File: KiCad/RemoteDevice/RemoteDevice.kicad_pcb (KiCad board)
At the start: 2 copper layers, 99.5 x 59.2 mm, 42 parts, among them J1 Alim, J2 CN1, Q1 Si4435, SW1 BP, SW2 BP, U1 XC9140, U2 STM32L041F6Px, U3 MCP6281, U4 ADT7410TRZ, U5 MCP6281, U6 RT606, U7 Microphone

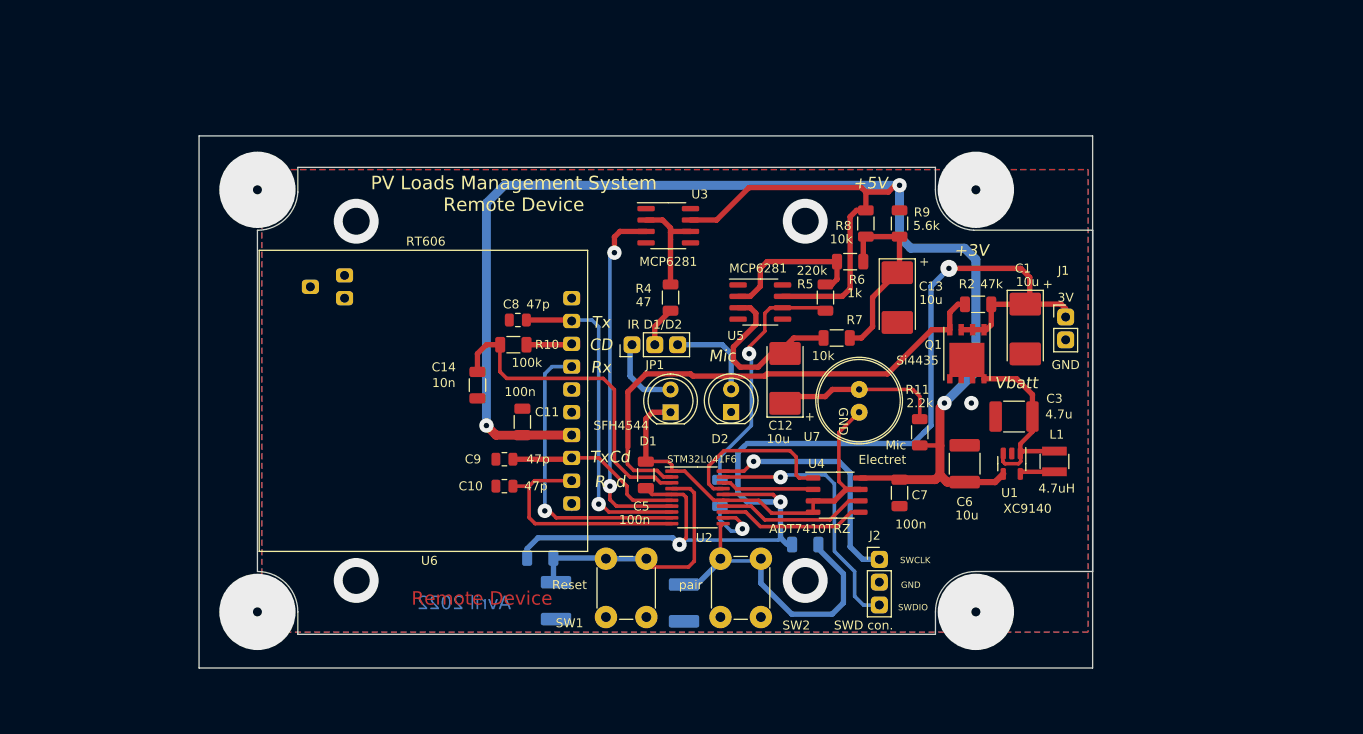
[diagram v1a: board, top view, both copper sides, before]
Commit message: routage commencé. ALim OK placer les deux diodes, étudier l'alim particulière uC et Temp Sensor
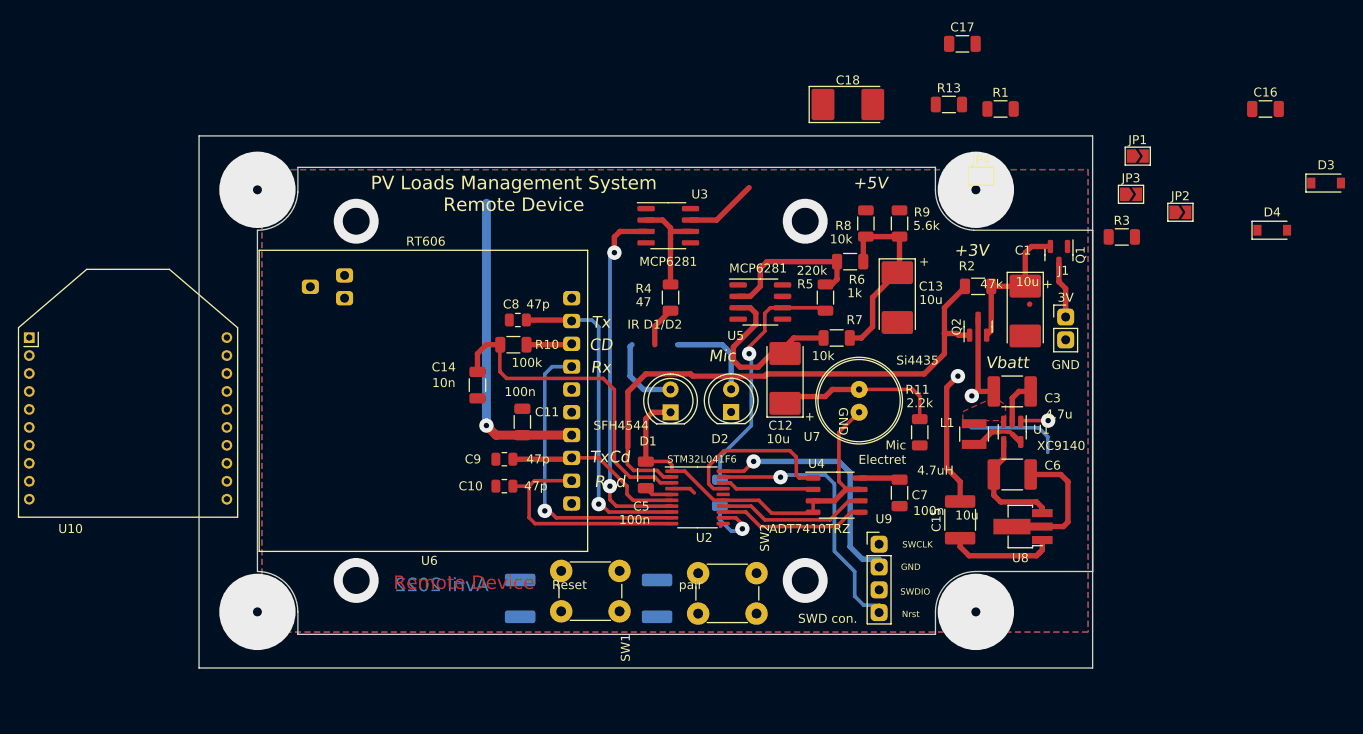
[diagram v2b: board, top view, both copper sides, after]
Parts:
- removed J2: CN1, LibKiCad_PjtDeviceManagePV:PinHeader3pts
- added C15: 10u, Capacitor_SMD:C_1812_4532Metric, F.Cu at (106.2, 102.2)
- added C16: 100n, Capacitor_SMD:C_1206_3216Metric, F.Cu at (140.2, 56.5)
- added C17: 10n, Capacitor_SMD:C_1206_3216Metric, F.Cu at (106.5, 49.2)
- added C18: 10u, Capacitor_Tantalum_SMD:CP_EIA-7132-20_AVX-U, F.Cu at (93.8, 56.0)
- added D3: BAT43W-V, Diode_SMD:D_SOD-123, F.Cu at (147.0, 64.8)
- added D4: BAT43W-V, Diode_SMD:D_SOD-123, F.Cu at (141.0, 70.0)
- added JP2: SolderJumper_2_Open, Jumper:SolderJumper-2_P1.3mm_Open_TrianglePad1.0x1.5mm, F.Cu at (130.8, 68.0)
- added JP3: SolderJumper_2_Open, Jumper:SolderJumper-2_P1.3mm_Open_TrianglePad1.0x1.5mm, F.Cu at (125.3, 66.0)
- added JP4: SolderJumper_2_Open, Jumper:SolderJumper-2_P1.3mm_Open_TrianglePad1.0x1.5mm, F.Cu at (108.6, 64.0)
- added Q2: Q_PMOS_GSD, Package_TO_SOT_SMD:SOT-23, F.Cu at (108.2, 80.8)
- added R13: 2.2k, Resistor_SMD:R_1206_3216Metric, F.Cu at (105.0, 56.0)
- added U10: XBEE-3, LibKiCad_INSA:XBEE-3-TH, F.Cu at (1.40, 102.0)
- added U8: LD2981CU33, Package_TO_SOT_SMD:SOT-89-3_Handsoldering, F.Cu at (113.2, 103.0)
- added U9: Con_4pts, LibKiCad_PjtDeviceManagePV:PinHeader4pts, F.Cu at (97.5, 107.8)
- JP1: value 3pts -> SolderJumper_2_Open; footprint LibKiCad_PjtDeviceManagePV:PinHeader3pts -> Jumper:SolderJumper-2_P1.3mm_Open_TrianglePad1.0x1.5mm
- Q1: value Si4435 -> Q_PMOS_GSD; footprint Package_SO:PowerPAK_SO-8_Single -> Package_TO_SOT_SMD:SOT-23
- R1: value R -> 10k; moved to F.Cu
- R3: value 4.7k -> 10k; moved to F.Cu
- moved R1 71.6 mm to (110.8, 56.5)
- moved JP1 57.7 mm to (126.0, 61.8), turned to 0 degrees
- moved R3 49.1 mm to (124.2, 70.8)
- moved Q1 15.0 mm to (117.2, 72.8)
- moved L1 9.46 mm to (107.8, 92.7)
- moved C6 5.43 mm to (112.0, 97.2), turned to 0 degrees
- moved SW1 4.03 mm to (65.0, 110.2), turned to 180 degrees
- moved C2 4.01 mm to (57.2, 111.0)
- moved U1 3.55 mm to (112.0, 92.5)
- moved C4 3.04 mm to (72.5, 111.0)
- moved C3 2.81 mm to (112.0, 88.0), turned to 0 degrees
- moved C1 2.00 mm to (113.5, 79.0)
- moved R2 2.00 mm to (108.2, 76.2)
- moved SW2 1.68 mm to (80.2, 110.5), turned to 180 degrees
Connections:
- C1 pad 1: +3V0 -> Net-(C1-Pad1)
- C5 pad 1: +3V0 -> VDD
- C7 pad 1: +5V -> /Pwr_ADT7410
- JP1 pad 1: /LED_Top -> /Pwr_ADT7410
- JP1 pad 2: /LED -> +3V3
- Q1 pad 1: +3V0 -> GND
- Q1 pad 2: +3V0 -> Net-(C1-Pad1)
- R1 pad 1: +3V0 -> /Pwr_ADT7410
- R1 pad 2: /Reset -> /SCL
- R11 pad 1: +5V -> Net-(C18-Pad1)
- R2 pad 1: +3V0 -> Net-(C1-Pad1)
- R3 pad 1: +3V0 -> /Pwr_ADT7410
- R3 pad 2: /UserBP -> /SDA
- R8 pad 1: +5V -> +3V3
- U2 pad 16: +3V0 -> VDD
- U2 pad 5: +3V0 -> VDD
- U3 pad 7: +5V -> +3V3
- U4 pad 8: +5V -> /Pwr_ADT7410
- U5 pad 7: +5V -> +3V3
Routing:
- net +5V: track 187.0 -> 47.7 mm, vias 3 -> 1
- net +3V0: track 131.6 -> 6.29 mm, vias 3 -> 0
- net /UserBP: track 35.2 -> 0.43 mm
- net GND: track 47.1 -> 79.2 mm
- net /Reset: track 29.7 -> 2.71 mm
- net +3V3: track 0.00 -> 20.1 mm
- net Net-(C1-Pad1): track 0.00 -> 16.3 mm
- net /BoostEn: track 56.4 -> 62.1 mm
- net /Vbatt: track 21.2 -> 26.3 mm, vias 0 -> 2
- net /Pwr_ADT7410: track 0.00 -> 4.45 mm
- net VDD: track 0.00 -> 3.18 mm
- net /Lx: track 3.90 -> 6.25 mm
- added copper zone on F.Cu, net /Vbatt
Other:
- board text added: "Nrst"

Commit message: Reste la partie Xbee et les résistances de pull up. Bien penser aussi les plans de masse alim...
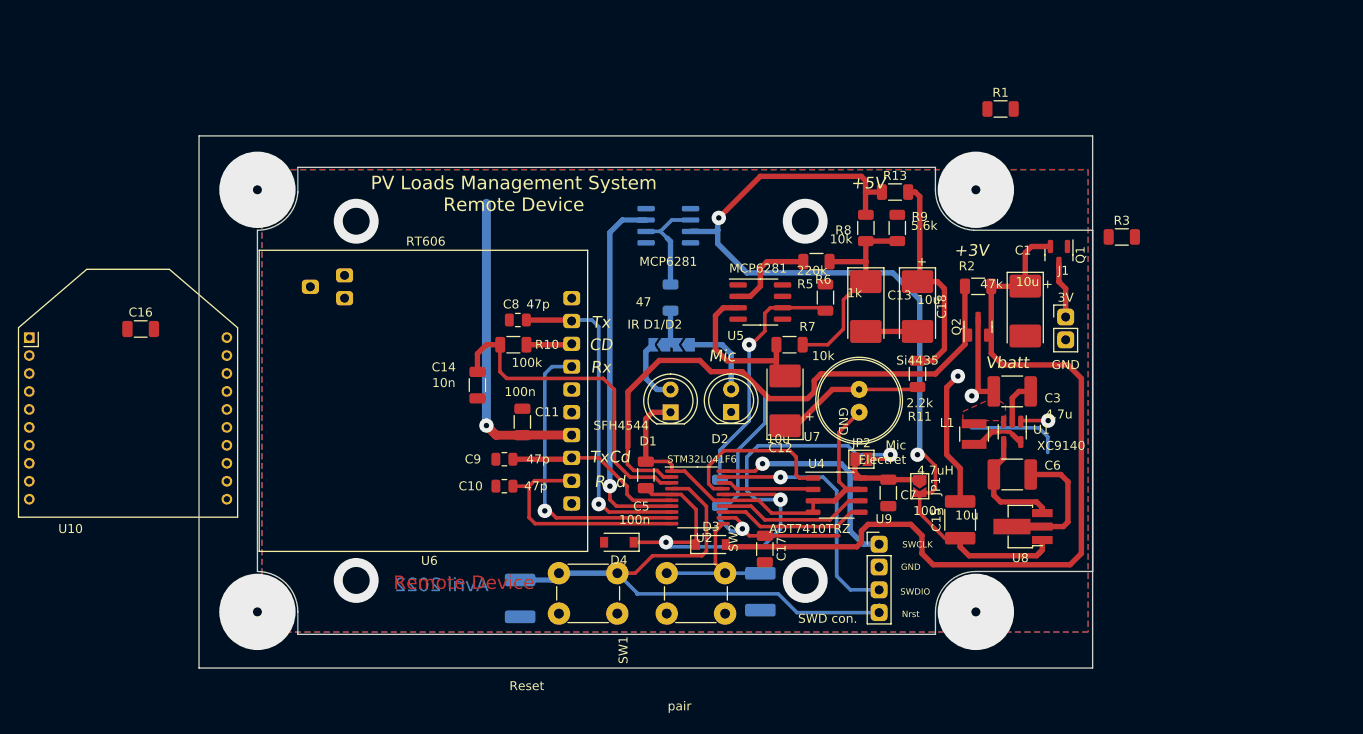
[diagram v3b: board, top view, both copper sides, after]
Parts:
- JP3, JP4, R4, U3: moved to B.Cu
- moved C16 127.6 mm to (15.0, 81.0)
- moved D4 80.6 mm to (68.2, 104.8), turned to 180 degrees
- moved D3 79.5 mm to (78.5, 105.0)
- moved C17 60.4 mm to (84.5, 105.5), turned to -90 degrees
- moved JP3 55.1 mm to (72.8, 82.8), turned to 180 degrees
- moved JP2 44.9 mm to (95.2, 95.5)
- moved JP1 44.0 mm to (101.8, 98.5), turned to -90 degrees
- moved JP4 38.1 mm to (75.5, 82.8), turned to 180 degrees
- moved C18 23.8 mm to (101.5, 78.5), turned to -90 degrees
- moved C4 11.5 mm to (84.0, 110.2)
- moved R13 11.4 mm to (99.0, 65.8)
- moved R11 6.50 mm to (101.5, 86.0), turned to -90 degrees
- moved R7 5.30 mm to (87.2, 82.8)
- moved R6 3.75 mm to (90.2, 73.5)
- moved C13 3.64 mm to (95.8, 78.5)
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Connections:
- net Net-(C1-Pad1) renamed /pile
- D1 pad 2: /LED_Top -> /LED_Side
- D2 pad 2: /LED_Side -> /LED_Top
- JP3 pad 2: /LED_Top -> /LED_Side
- JP4 pad 1: /LED_Side -> /LED_Top
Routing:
- net +3V3: track 20.1 -> 99.9 mm, vias 0 -> 2
- net /pile: track 16.3 -> 94.5 mm
- net VDD: track 3.18 -> 68.8 mm, vias 0 -> 3
- net /Reset: track 2.71 -> 63.3 mm
- net /MicroPhone: track 7.74 -> 33.8 mm
- net Net-(C18-Pad1): track 0.00 -> 24.7 mm
- net /UserBP: track 0.43 -> 16.7 mm
- net /CR_AOP: track 17.3 -> 10.0 mm
- net GND: track 79.2 -> 85.0 mm
- net /Pwr_ADT7410: track 4.45 -> 9.04 mm
- net /LED_Side: track 10.3 -> 7.31 mm
- net /VtGND: track 21.0 -> 23.9 mm
- net /MiC: track 18.2 -> 15.9 mm
- net /MIC_InAOP: track 19.9 -> 17.8 mm
- net /SWCLK: track 27.2 -> 25.2 mm
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
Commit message: Routage presque fini, reprendre la partie bottom en niveau de la sériegraphie
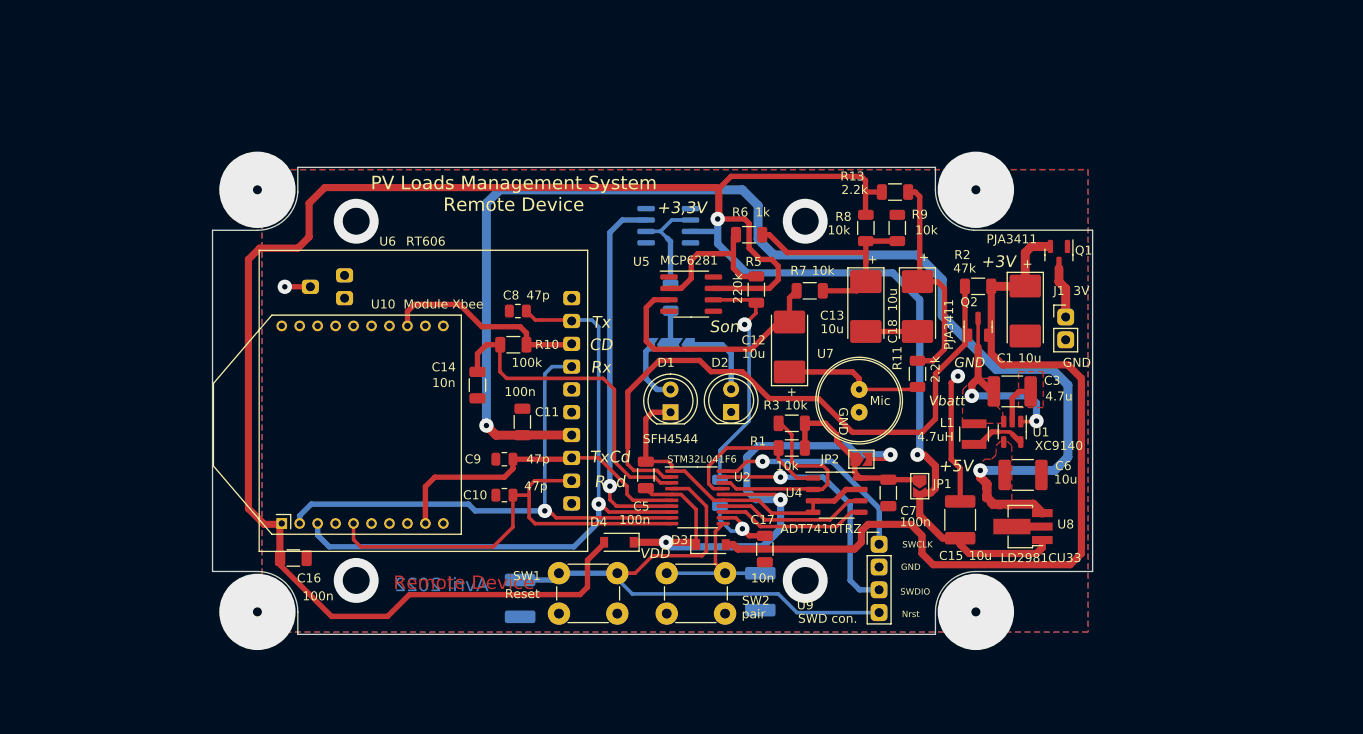
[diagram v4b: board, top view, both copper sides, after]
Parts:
- moved U10 49.3 mm to (50.7, 103.9), turned to 90 degrees
- moved R1 44.3 mm to (87.5, 94.2), turned to 180 degrees
- moved R3 42.2 mm to (87.5, 91.5), turned to 180 degrees
- moved C16 30.6 mm to (32.0, 106.5)
- moved R6 8.08 mm to (82.8, 70.5)
- moved R5 7.75 mm to (83.6, 76.6)
- moved U5 7.75 mm to (76.3, 77.1)
- moved R7 6.41 mm to (89.5, 76.8)
- moved C12 6.02 mm to (87.2, 83.0)
- moved C6 1.20 mm to (113.2, 97.2)
- moved C10 1.00 mm to (55.5, 99.5)
- moved C8 1.00 mm to (57.0, 79.0)
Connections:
- net Net-(R12-Pad1) renamed /Son
- C1 pad 1: /pile -> +3V0
- D3 pad 2: /pile -> +3V0
- J1 pad 1: +3V0 -> /piles
- Q1 pad 2: /pile -> +3V0
- Q1 pad 3: +3V0 -> /piles
- Q2 pad 2: /pile -> +3V0
- R2 pad 1: /pile -> +3V0
- U6 pad 11: unconnected-(U6-Pad11) -> /Ant
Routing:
- net +3V3: track 99.9 -> 259.0 mm
- net +5V: track 47.7 -> 142.2 mm, vias 1 -> 2
- net /pile: track 94.5 -> 0.00 mm
- net +3V0: track 6.29 -> 95.1 mm
- net /DataIn: track 36.7 -> 73.4 mm
- net /DataOut: track 33.0 -> 62.0 mm
- net /RxCmde: track 26.5 -> 50.8 mm
- net /MicroPhone: track 33.8 -> 10.6 mm
- net GND: track 85.0 -> 62.5 mm
- net /CD: track 5.07 -> 22.9 mm
- net /TxCmde: track 20.2 -> 36.0 mm
- net /SDA: track 10.3 -> 22.9 mm
- net /Pwr_ADT7410: track 9.04 -> 19.4 mm
- net /MIC_InAOP: track 17.8 -> 28.0 mm
- net /CR_AOP: track 10.0 -> 16.8 mm
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- added copper zone on F.Cu, net +5V
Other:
- board size 99.5 x 59.2 mm -> 98 x 52 mm
- board text added: "+3,3V"
- board text added: "LD2981CU33"
- board text added: "Module Xbee"
- board text added: "PJA3411"
- board text added: "Son"
- board text added: "VDD"
- board text removed: "47"
- board text removed: "5.6k"
- board text removed: "IR D1/D2"
- board text removed: "Mic Electret"
- board text removed: "Si4435"

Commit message: routage terminé, proto à envoyer à José
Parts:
- added J2: pin, LibKiCad_PjtDeviceManagePV:PinHeader1Pt, F.Cu at (117.5, 83.2)
- J1: value Alim -> pin; footprint LibKiCad_PjtDeviceManagePV:PinHeader2pts -> LibKiCad_PjtDeviceManagePV:PinHeader1Pt
- Q1, Q2: value Q_PMOS_GSD -> PJA3411
- R9: value 5.6k -> 10k
- moved J1 3.31 mm to (117.5, 79.0)
- moved Q1 2.26 mm to (117.5, 75.0)
- moved R7 1.00 mm to (90.5, 76.8)
- moved R8 1.00 mm to (95.8, 70.8)
- moved C12 0.75 mm to (88.0, 83.0)
- moved JP3 0.75 mm to (72.0, 82.8)
- moved R13 0.75 mm to (99.0, 66.5)
- moved R9 0.75 mm to (99.2, 70.5)
- moved JP4 0.50 mm to (76.0, 82.8)
- moved C1 0.25 mm to (113.2, 79.0)
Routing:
- net +3V0: track 95.1 -> 101.8 mm
- net /piles: track 6.29 -> 3.13 mm
- net /VtGND: track 25.6 -> 23.7 mm
- net /LED: track 4.67 -> 6.37 mm
- net /LED_Side: track 7.31 -> 6.26 mm
- net /BoostEn: track 69.3 -> 68.2 mm
- net /MIC_InAOP: track 28.0 -> 27.1 mm
- net /DataIn: track 73.4 -> 74.2 mm
- net /MiC: track 15.3 -> 14.5 mm
- net +5V: track 142.2 -> 141.5 mm
- net +3V3: track 259.0 -> 259.6 mm
- net GND: vias 1 -> 5
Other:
- outline, holes or cut-outs redrawn
- board text added: "47"
- board text added: "BAT43"

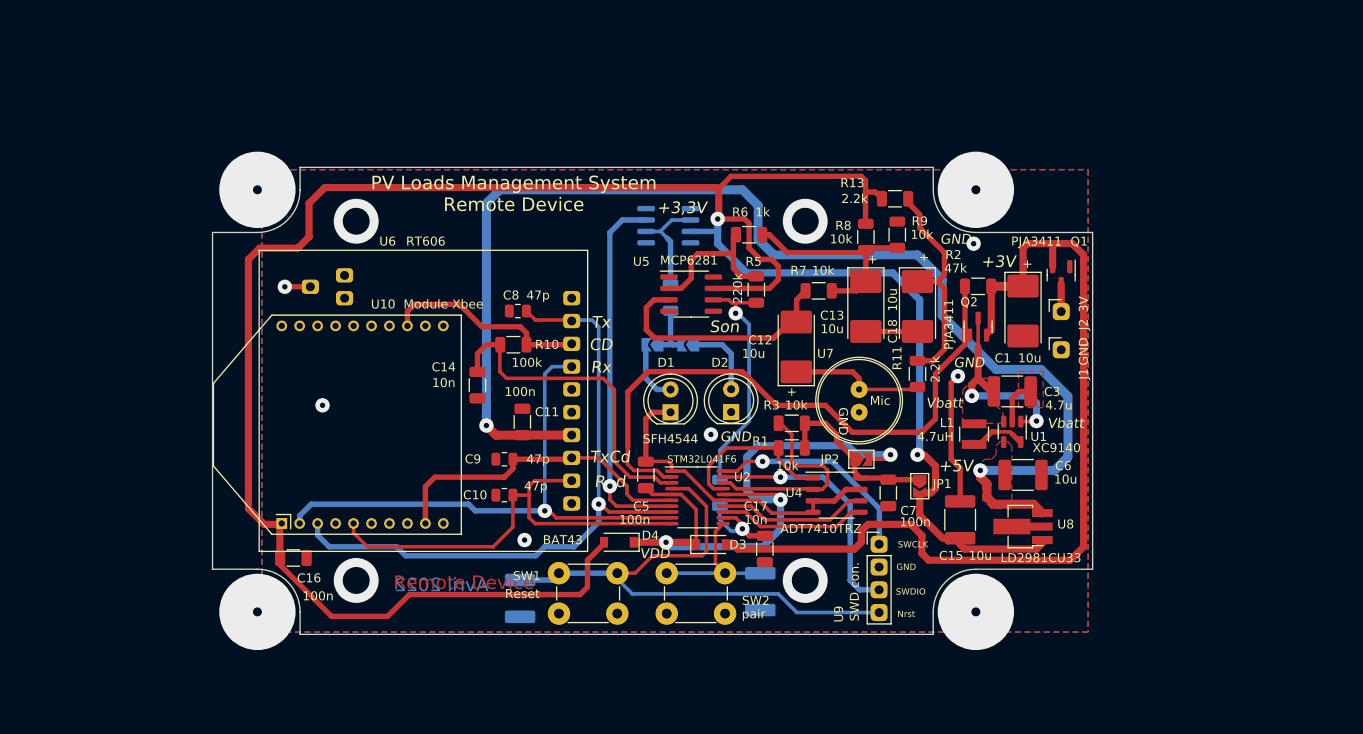
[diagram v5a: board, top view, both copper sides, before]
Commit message: Routage revu (tailles condensateur sur switchs). Version envoyée à José le 20 06 2022
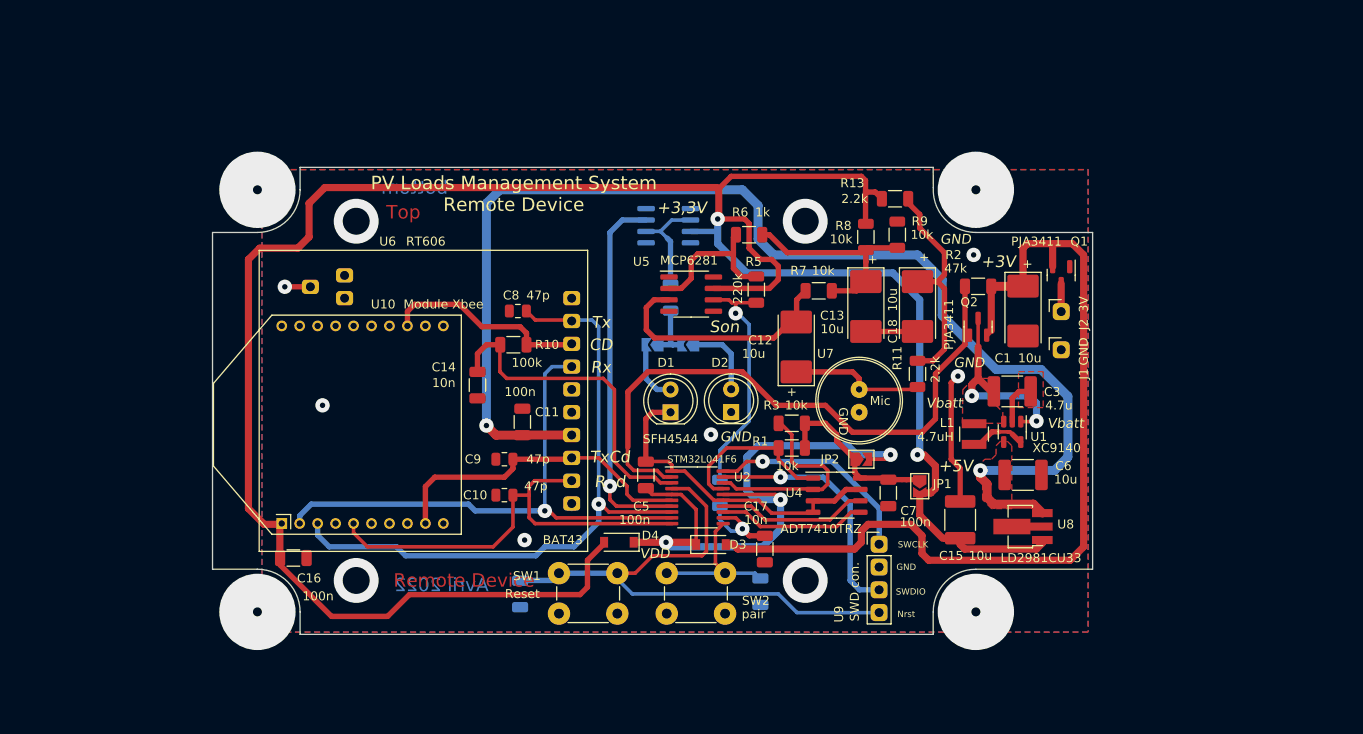
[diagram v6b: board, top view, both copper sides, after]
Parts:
- C2, C4: value 2.2u -> 100n; footprint Capacitor_SMD:C_1812_4532Metric -> Capacitor_SMD:C_1206_3216Metric
- moved C2 0.50 mm to (57.2, 110.5)
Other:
- board text added: "Top"
- board text added: "bottom"
- board text removed: "2.2u"
